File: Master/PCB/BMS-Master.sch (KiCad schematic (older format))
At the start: 30 parts, among them J1 BAT, J10 Charge, J11 CAN, J12 USB, J13 Discharge, J14 Corner, J15 Corner, J18 OLED, J19 Master, J2 Charge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

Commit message: PCB master update
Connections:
- net GNDA: now also J2.2 (Pin_2); no longer J2.1 (Pin_1)
- net PowerMonitor/Charge+: now also J2.1 (Pin_1); no longer J2.2 (Pin_2)
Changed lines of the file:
@@
 F9 "Vpack" I R 6100 1850 50
 F10 "ChargeDetect" B R 6100 2350 50
+F11 "24V" I R 6100 2450 50
 $EndSheet
 NoConn ~ 4000 2200
@@
 	7150 4800 6250 4800
 Wire Wire Line
-	6100 3300 6650 3300
+	6100 3300 6250 3300
 Wire Wire Line
 	6650 3300 6650 2850
@@
 F5 "ExternalPower" I L 4350 3600 50
 F6 "ChargeDetect" I R 6100 3800 50
-F7 "24V" I R 6100 3300 50
+F7 "24V" O R 6100 3300 50
 F8 "EnableFromExt" I R 6100 3500 50
 $EndSheet
@@
 	1    9800 2500
 	1    0    0    -1
-$EndComp
-$Comp
-L Connector_Generic:Conn_01x02 J2
-U 1 1 5C3822E8
-P 14400 1050
-F 0 "J2" H 14480 1042 50  0000 L CNN
-F 1 "Charge" H 14480 951 50  0000 L CNN
-F 2 "TerminalBlock_RND:TerminalBlock_RND_205-00001_Pitch5.00mm" H 14400 1050 50  0001 C CNN
-F 3 "~" H 14400 1050 50  0001 C CNN
-	1    14400 1050
-	1    0    0    1
 $EndComp
 $Comp
@@
 	1    0    0    -1
 $EndComp
+$Comp
+L Connector_Generic:Conn_01x02 J2
+U 1 1 5C3822E8
+P 14400 950
+F 0 "J2" H 14480 942 50  0000 L CNN
+F 1 "Charge" H 14480 851 50  0000 L CNN
+F 2 "TerminalBlock_RND:TerminalBlock_RND_205-00001_Pitch5.00mm" H 14400 950 50  0001 C CNN
+F 3 "~" H 14400 950 50  0001 C CNN
+	1    14400 950
+	1    0    0    -1
+$EndComp
+Wire Wire Line
+	6100 2450 6250 2450
+Wire Wire Line
+	6250 2450 6250 3300
+Connection ~ 6250 3300
+Wire Wire Line
+	6250 3300 6650 3300
 $EndSCHEMATC

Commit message: small corections
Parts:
- R42, R46, R50: value 4.75 -> 4.75k
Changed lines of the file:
@@
 P 10250 8850
 F 0 "R50" V 10450 8850 50  0000 C CNN
-F 1 "4.75" V 10350 8850 50  0000 C CNN
+F 1 "4.75k" V 10350 8850 50  0000 C CNN
 F 2 "Resistors_SMD:R_0603_HandSoldering" V 10180 8850 50  0001 C CNN
 F 3 "~" H 10250 8850 50  0001 C CNN
@@
 P 9850 8850
 F 0 "R42" V 10050 8850 50  0000 C CNN
-F 1 "4.75" V 9950 8850 50  0000 C CNN
+F 1 "4.75k" V 9950 8850 50  0000 C CNN
 F 2 "Resistors_SMD:R_0603_HandSoldering" V 9780 8850 50  0001 C CNN
 F 3 "~" H 9850 8850 50  0001 C CNN
@@
 P 10000 9600
 F 0 "R46" V 10200 9600 50  0000 C CNN
-F 1 "4.75" V 10100 9600 50  0000 C CNN
+F 1 "4.75k" V 10100 9600 50  0000 C CNN
 F 2 "Resistors_SMD:R_0603_HandSoldering" V 9930 9600 50  0001 C CNN
 F 3 "~" H 10000 9600 50  0001 C CNN

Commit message: Small changes on master
Possible now to bypass  isolation & PSU if only one slave is used.
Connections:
- net PowerMonitor/I-: now reaches J7.3 (Pin_3)
- net PowerMonitor/I renamed PowerMonitor/I+
- no-connect marks 6 -> 5
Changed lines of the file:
@@
 F0 "PowerMonitor" 50
 F1 "PowerMonitor.sch" 50
-F2 "I" I L 4350 2100 50
+F2 "I+" I L 4350 2100 50
 F3 "SCL" I R 6100 2050 50
 F4 "SDA" I R 6100 2150 50
@@
 F10 "ChargeDetect" B R 6100 2350 50
 F11 "24V" I R 6100 2450 50
+F12 "I-" I L 4350 2200 50
 $EndSheet
-NoConn ~ 4000 2200
 $Comp
 L power:GNDA #PWR0115
@@
 Wire Wire Line
 	6250 3300 6650 3300
+Wire Wire Line
+	4000 2200 4350 2200
 $EndSCHEMATC

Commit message: readme
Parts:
- F1: value Fuse -> 5A
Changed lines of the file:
@@
 Wire Wire Line
 	9500 2300 10100 2300
-$Comp
-L BMS-Master-rescue:Fuse-Device F1
-U 1 1 5ACF057B
-P 4050 3600
-F 0 "F1" V 3800 3600 50  0000 C CNN
-F 1 "Fuse" V 3900 3600 50  0000 C CNN
-F 2 "Fuse_Holders_and_Fuses:Fuse_SMD1206_HandSoldering" V 3980 3600 50  0001 C CNN
-F 3 "~" H 4050 3600 50  0001 C CNN
-	1    4050 3600
-	0    -1   1    0
-$EndComp
 $Sheet
 S 9250 6450 1600 750
@@
 	7150 4800 6250 4800
 Wire Wire Line
-	6100 3300 6250 3300
-Wire Wire Line
 	6650 3300 6650 2850
 Wire Wire Line
 	6650 2850 7150 2850
-$Sheet
-S 4350 3200 1750 950
-U 5AC18063
-F0 "PowerSupply" 50
-F1 "PowerSupply.sch" 50
-F2 "PushButton" I L 4350 3900 50
-F3 "PowerButton" I R 6100 4000 50
-F4 "PowerEnable" I R 6100 3900 50
-F5 "ExternalPower" I L 4350 3600 50
-F6 "ChargeDetect" I R 6100 3800 50
-F7 "24V" O R 6100 3300 50
-F8 "EnableFromExt" I R 6100 3500 50
-$EndSheet
 Wire Wire Line
 	6150 4950 7150 4950
@@
 Wire Wire Line
 	6150 4350 6150 4950
-Wire Wire Line
-	3900 3600 3650 3600
 Text Notes 1650 2050 0    200  ~ 40
 ISOLATED
@@
 	6100 2450 6250 2450
 Wire Wire Line
+	6250 3300 6650 3300
+Wire Wire Line
+	4000 2200 4350 2200
+$Comp
+L BMS-Master-rescue:Fuse-Device F1
+U 1 1 5ACF057B
+P 4050 3600
+F 0 "F1" V 3800 3600 50  0000 C CNN
+F 1 "5A" V 3900 3600 50  0000 C CNN
+F 2 "Fuse_Holders_and_Fuses:Fuse_SMD1206_HandSoldering" V 3980 3600 50  0001 C CNN
+F 3 "~" H 4050 3600 50  0001 C CNN
+	1    4050 3600
+	0    -1   1    0
+$EndComp
+Connection ~ 6250 3300
+Wire Wire Line
+	6100 3300 6250 3300
+$Sheet
+S 4350 3200 1750 950
+U 5AC18063
+F0 "PowerSupply" 50
+F1 "PowerSupply.sch" 50
+F2 "PushButton" I L 4350 3900 50
+F3 "PowerButton" I R 6100 4000 50
+F4 "PowerEnable" I R 6100 3900 50
+F5 "ExternalPower" I L 4350 3600 50
+F6 "ChargeDetect" I R 6100 3800 50
+F7 "24V" O R 6100 3300 50
+F8 "EnableFromExt" I R 6100 3500 50
+$EndSheet
+Wire Wire Line
 	6250 2450 6250 3300
-Connection ~ 6250 3300
-Wire Wire Line
-	6250 3300 6650 3300
-Wire Wire Line
-	4000 2200 4350 2200
+Wire Wire Line
+	3900 3600 3650 3600
 $EndSCHEMATC

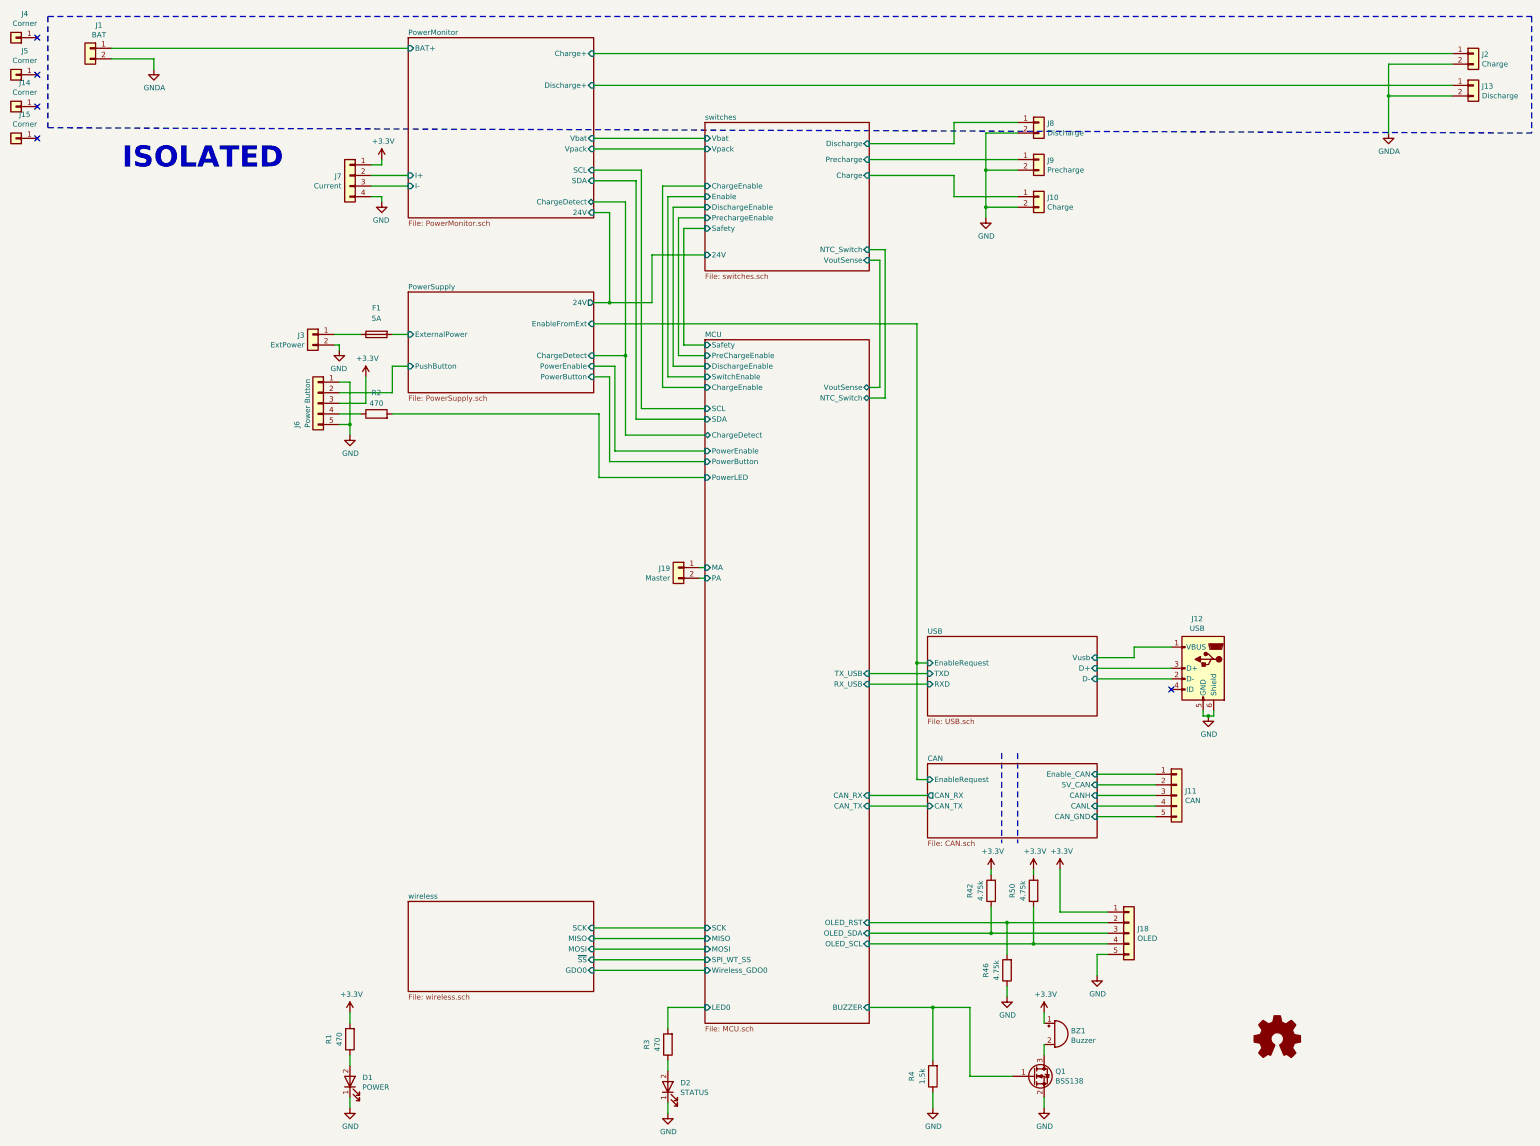
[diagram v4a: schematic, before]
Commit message: New buzzer, new connector & mistake correction
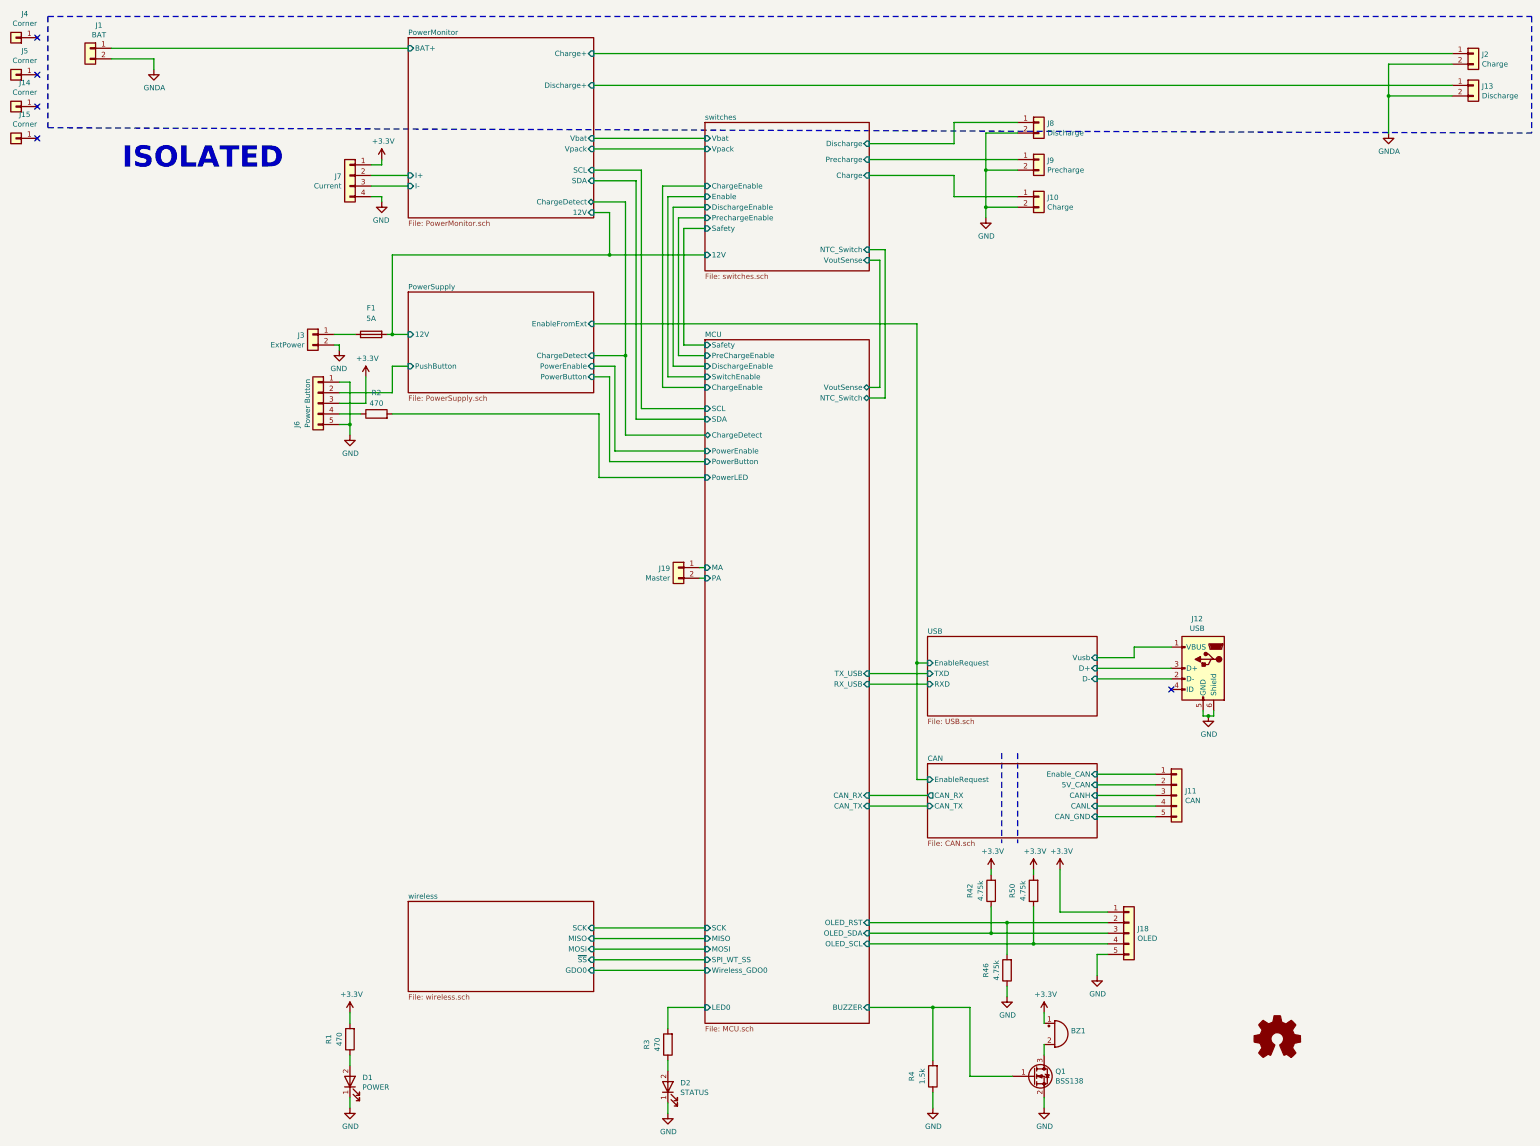
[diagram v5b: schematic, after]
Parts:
- BZ1: value Buzzer -> AI-1027-TWT-5V; footprint Buzzers_Beepers:PUIAudio_SMT_0825_S_4_R -> ENNOID:BUZZER
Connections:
- net PowerSupply/ExternalPower renamed PowerMonitor/12V
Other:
- moved on the sheet: F1
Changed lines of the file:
@@
 P 10450 10200
 F 0 "BZ1" H 10603 10229 50  0000 L CNN
-F 1 "Buzzer" H 10603 10138 50  0000 L CNN
-F 2 "Buzzers_Beepers:PUIAudio_SMT_0825_S_4_R" V 10425 10300 50  0001 C CNN
+F 1 "AI-1027-TWT-5V" H 10603 10138 50  0001 L CNN
+F 2 "ENNOID:BUZZER" V 10425 10300 50  0001 C CNN
 F 3 "~" V 10425 10300 50  0001 C CNN
 	1    10450 10200
@@
 F10 "Vpack" I L 7150 1850 50
 F11 "Vbat" I L 7150 1750 50
-F12 "24V" I L 7150 2850 50
+F12 "12V" I L 7150 2850 50
 F13 "VoutSense" I R 8700 2900 50
 F14 "NTC_Switch" I R 8700 2800 50
@@
 F9 "Vpack" I R 6100 1850 50
 F10 "ChargeDetect" B R 6100 2350 50
-F11 "24V" I R 6100 2450 50
+F11 "12V" I R 6100 2450 50
 F12 "I-" I L 4350 2200 50
 $EndSheet
@@
 Wire Wire Line
 	7150 4800 6250 4800
-Wire Wire Line
-	6650 3300 6650 2850
-Wire Wire Line
-	6650 2850 7150 2850
 Wire Wire Line
 	6150 4950 7150 4950
@@
 	6100 2450 6250 2450
 Wire Wire Line
-	6250 3300 6650 3300
-Wire Wire Line
 	4000 2200 4350 2200
 $Comp
 L BMS-Master-rescue:Fuse-Device F1
 U 1 1 5ACF057B
-P 4050 3600
-F 0 "F1" V 3800 3600 50  0000 C CNN
-F 1 "5A" V 3900 3600 50  0000 C CNN
-F 2 "Fuse_Holders_and_Fuses:Fuse_SMD1206_HandSoldering" V 3980 3600 50  0001 C CNN
-F 3 "~" H 4050 3600 50  0001 C CNN
-	1    4050 3600
+P 4000 3600
+F 0 "F1" V 3750 3600 50  0000 C CNN
+F 1 "5A" V 3850 3600 50  0000 C CNN
+F 2 "Fuse_Holders_and_Fuses:Fuse_SMD1206_HandSoldering" V 3930 3600 50  0001 C CNN
+F 3 "~" H 4000 3600 50  0001 C CNN
+	1    4000 3600
 	0    -1   1    0
 $EndComp
-Connection ~ 6250 3300
-Wire Wire Line
-	6100 3300 6250 3300
+Connection ~ 6250 2850
 $Sheet
 S 4350 3200 1750 950
@@
 F3 "PowerButton" I R 6100 4000 50
 F4 "PowerEnable" I R 6100 3900 50
-F5 "ExternalPower" I L 4350 3600 50
+F5 "12V" I L 4350 3600 50
 F6 "ChargeDetect" I R 6100 3800 50
-F7 "24V" O R 6100 3300 50
-F8 "EnableFromExt" I R 6100 3500 50
+F7 "EnableFromExt" I R 6100 3500 50
 $EndSheet
 Wire Wire Line
-	6250 2450 6250 3300
-Wire Wire Line
-	3900 3600 3650 3600
+	6250 2450 6250 2850
+Wire Wire Line
+	3850 3600 3650 3600
+Wire Wire Line
+	6250 2850 7150 2850
+Wire Wire Line
+	4200 2850 4200 3600
+Wire Wire Line
+	4200 2850 6250 2850
+Connection ~ 4200 3600
+Wire Wire Line
+	4200 3600 4150 3600
 $EndSCHEMATC

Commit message: nothing
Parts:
- J11: footprint Connectors_Molex:Molex_PicoBlade_53261-0571_05x1.25mm_Angled -> Connectors_Molex:Molex_KK-6410-05_05x2.54mm_Straight
- J18, J6: footprint Connectors_Molex:Molex_PicoBlade_53398-0571_05x1.25mm_Straight -> Connectors_Molex:Molex_KK-6410-05_05x2.54mm_Straight
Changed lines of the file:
@@
-EESchema Schematic File Version 4
+EESchema Schematic File Version 5
 LIBS:BMS-Master-cache
 EELAYER 29 0
@@
 F 0 "J6" V 3700 4050 50  0000 C CNN
 F 1 "Power Button" V 3600 4250 50  0000 C CNN
-F 2 "Connectors_Molex:Molex_PicoBlade_53398-0571_05x1.25mm_Straight" H 3500 4250 50  0001 C CNN
+F 2 "Connectors_Molex:Molex_KK-6410-05_05x2.54mm_Straight" H 3500 4250 50  0001 C CNN
 F 3 "~" H 3500 4250 50  0001 C CNN
 	1    3500 4250
@@
 F 0 "J11" H 11680 7992 50  0000 L CNN
 F 1 "CAN" H 11680 7901 50  0000 L CNN
-F 2 "Connectors_Molex:Molex_PicoBlade_53261-0571_05x1.25mm_Angled" H 11600 7950 50  0001 C CNN
+F 2 "Connectors_Molex:Molex_KK-6410-05_05x2.54mm_Straight" H 11600 7950 50  0001 C CNN
 F 3 "" H 11600 7950 50  0001 C CNN
 	1    11600 7950
@@
 F 0 "J18" H 11230 9292 50  0000 L CNN
 F 1 "OLED" H 11230 9201 50  0000 L CNN
-F 2 "Connectors_Molex:Molex_PicoBlade_53398-0571_05x1.25mm_Straight" H 11150 9250 50  0001 C CNN
+F 2 "Connectors_Molex:Molex_KK-6410-05_05x2.54mm_Straight" H 11150 9250 50  0001 C CNN
 F 3 "" H 11150 9250 50  0001 C CNN
 	1    11150 9250

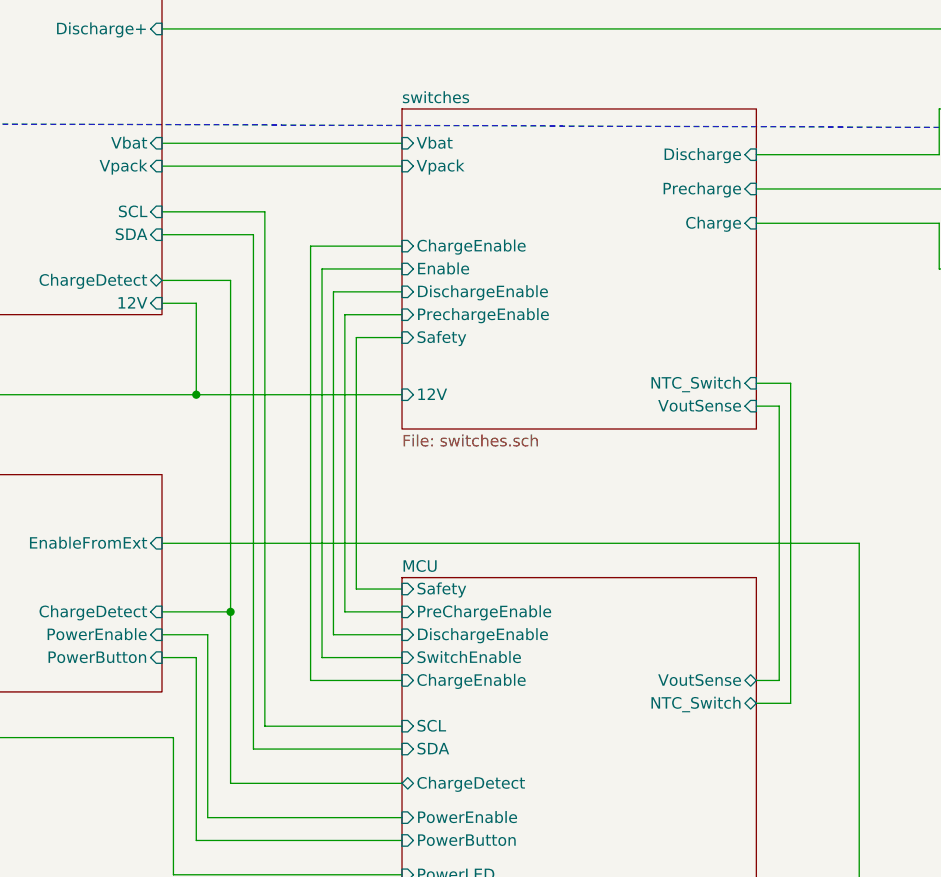
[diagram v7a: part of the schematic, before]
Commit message: schematics major improvement by removing bq76200
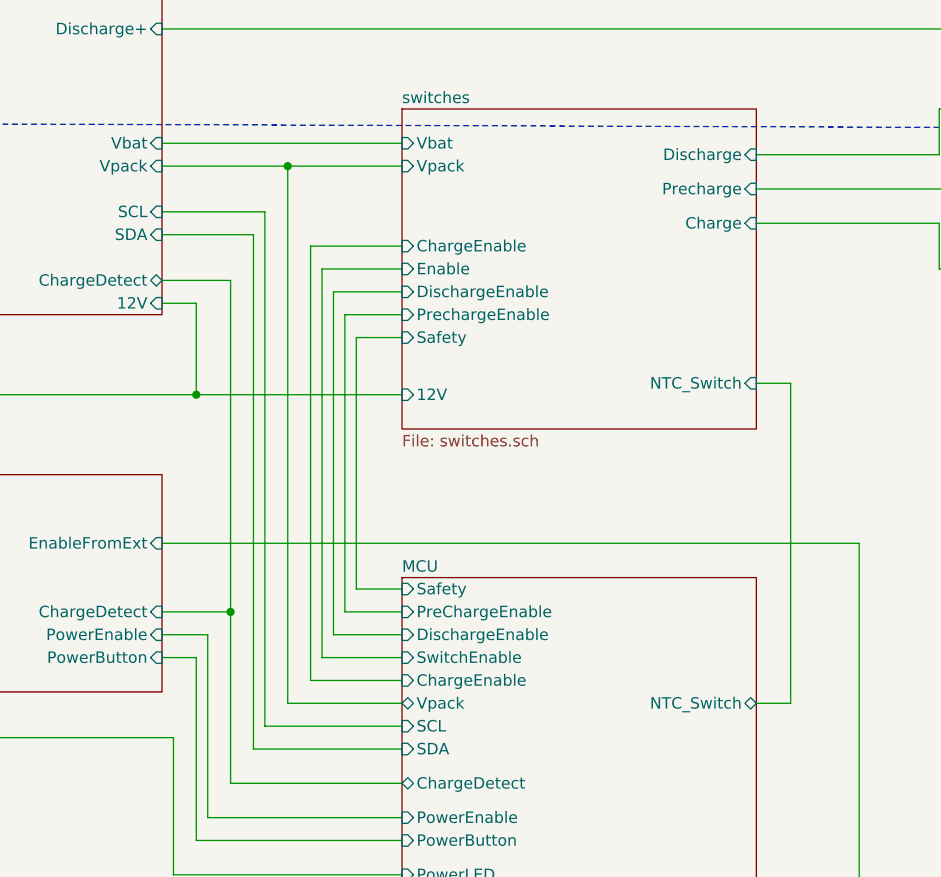
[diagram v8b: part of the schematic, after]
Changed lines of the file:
@@
 F11 "Vbat" I L 7150 1750 50
 F12 "12V" I L 7150 2850 50
-F13 "VoutSense" I R 8700 2900 50
-F14 "NTC_Switch" I R 8700 2800 50
+F13 "NTC_Switch" I R 8700 2800 50
 $EndSheet
 $Comp
@@
 	6100 1750 7150 1750
 Wire Wire Line
-	6100 1850 7150 1850
-Wire Wire Line
 	14200 950  6100 950
 Wire Wire Line
@@
 	9150 7800 9250 7800
 Connection ~ 9150 6700
-Wire Wire Line
-	8700 4100 8800 4100
-Wire Wire Line
-	8800 4100 8800 2900
-Wire Wire Line
-	8800 2900 8700 2900
 Wire Wire Line
 	8700 2800 8850 2800
@@
 F14 "RX_USB" I R 8700 6900 50
 F15 "Safety" I L 7150 3700 50
-F16 "VoutSense" B R 8700 4100 50
+F16 "Vpack" B L 7150 4200 50
 F17 "SCK" I L 7150 9200 50
 F18 "MISO" I L 7150 9300 50
@@
 Wire Wire Line
 	4200 3600 4150 3600
+Wire Wire Line
+	6100 1850 6650 1850
+Wire Wire Line
+	7150 4200 6650 4200
+Wire Wire Line
+	6650 4200 6650 1850
+Connection ~ 6650 1850
+Wire Wire Line
+	6650 1850 7150 1850
 $EndSCHEMATC
